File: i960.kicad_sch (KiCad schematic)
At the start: 48 parts

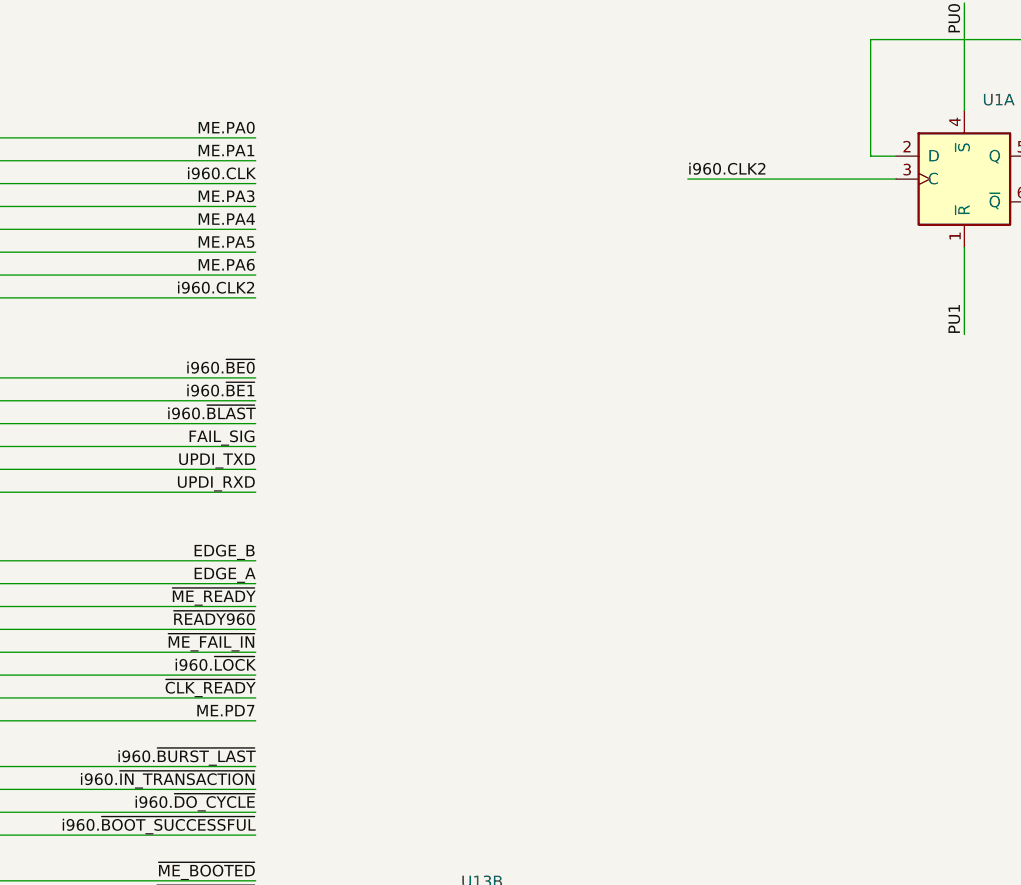
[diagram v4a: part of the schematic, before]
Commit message: Added a new 9 pin breakout header for me pins
PORTA on the ME is now free. CLK is now connected to PD7. That way I can
reuse all of PORTA for whatever I want in the future.
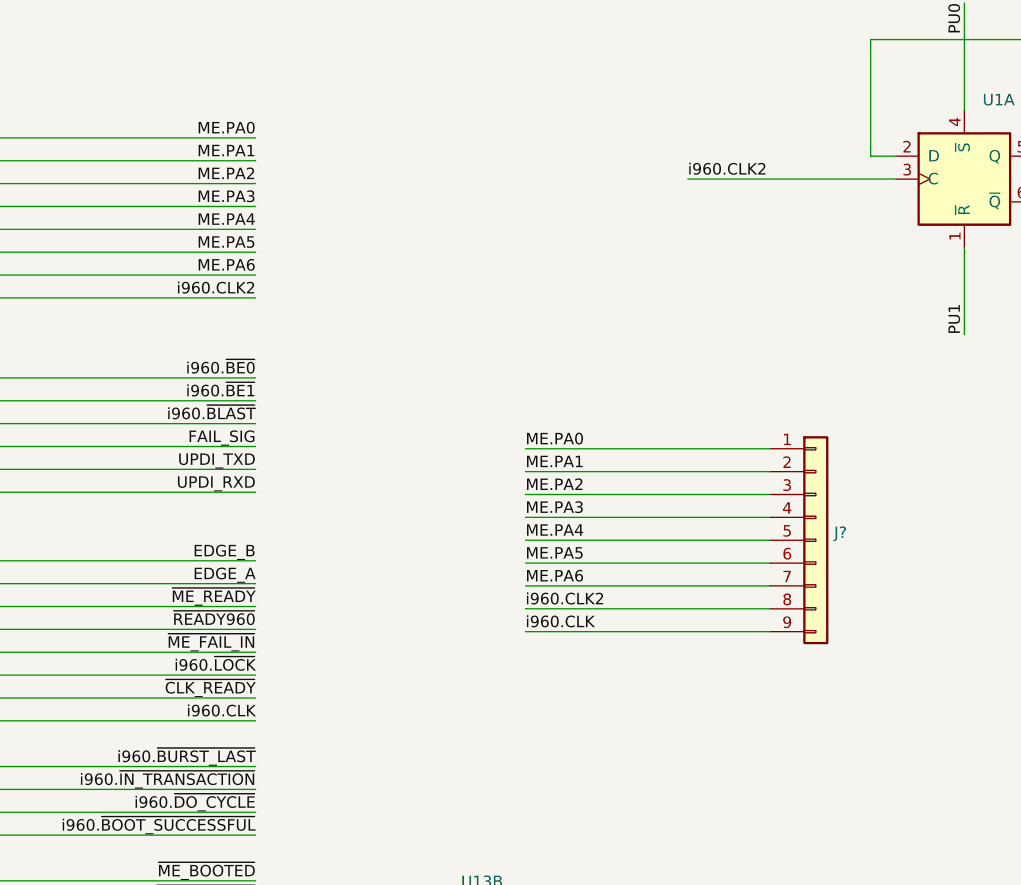
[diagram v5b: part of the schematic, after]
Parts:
- added J?: (no value), symbol Connector_Generic:Conn_01x09
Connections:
- net ME.PD7 is gone; now on net i960.CLK: U16.16 ((AIN7/AREF)PD7)
- net ME.PA0: now also J?.1 (Pin_1)
- net ME.PA1: now also J?.2 (Pin_2)
- net ME.PA3: now also J?.4 (Pin_4)
- net ME.PA4: now also J?.5 (Pin_5)
- net ME.PA5: now also J?.6 (Pin_6)
- net ME.PA6: now also J?.7 (Pin_7)
- net i960.CLK: now also J?.9 (Pin_9); no longer U16.35 ((XCK0/SDA/CCL0-IN2)PA2)
- net i960.CLK2: now also J?.8 (Pin_8)
- new net ME.PA2: J?.3 (Pin_3), U16.35 ((XCK0/SDA/CCL0-IN2)PA2)
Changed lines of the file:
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@@
+    (stroke (width 0) (type default) (color 0 0 0 0))
+  )
+  (wire (pts (xy 172.466 84.582) (xy 199.644 84.582))
     (stroke (width 0) (type default) (color 0 0 0 0))
   )
@@
     (stroke (width 0) (type default) (color 0 0 0 0))
   )
+  (wire (pts (xy 172.466 76.962) (xy 199.644 76.962))
+    (stroke (width 0) (type default) (color 0 0 0 0))
+  )
   (wire (pts (xy 514.604 80.264) (xy 542.29 80.264))
     (stroke (width 0) (type default) (color 0 0 0 0))
@@
     (stroke (width 0) (type default) (color 0 0 0 0))
   )
+  (wire (pts (xy 172.466 89.662) (xy 199.644 89.662))
+    (stroke (width 0) (type default) (color 0 0 0 0))
+  )
   (wire (pts (xy 45.212 135.128) (xy 45.212 118.11))
     (stroke (width 0) (type default) (color 0 0 0 0))
@@
     (stroke (width 0) (type default) (color 0 0 0 0))
   )
+  (wire (pts (xy 172.466 79.502) (xy 199.644 79.502))
+    (stroke (width 0) (type default) (color 0 0 0 0))
+  )
   (wire (pts (xy 210.312 462.788) (xy 210.312 427.736))
     (stroke (width 0) (type default) (color 0 0 0 0))
@@
     (stroke (width 0) (type default) (color 0 0 0 0))
   )
+  (wire (pts (xy 172.466 97.282) (xy 199.644 97.282))
+    (stroke (width 0) (type default) (color 0 0 0 0))
+  )
   (wire (pts (xy 59.69 61.468) (xy 20.066 61.468))
     (stroke (width 0) (type default) (color 0 0 0 0))
@@
     (stroke (width 0) (type default) (color 0 0 0 0))
   )
+  (wire (pts (xy 172.466 82.042) (xy 199.644 82.042))
+    (stroke (width 0) (type default) (color 0 0 0 0))
+  )
   (wire (pts (xy 23.876 364.236) (xy 54.102 364.236))
     (stroke (width 0) (type default) (color 0 0 0 0))
@@
     (stroke (width 0) (type default) (color 0 0 0 0))
   )
+  (wire (pts (xy 172.466 94.742) (xy 199.644 94.742))
+    (stroke (width 0) (type default) (color 0 0 0 0))
+  )
   (wire (pts (xy 467.106 57.404) (xy 502.92 57.404))
     (stroke (width 0) (type default) (color 0 0 0 0))
@@
     (stroke (width 0) (type default) (color 0 0 0 0))
   )
+  (wire (pts (xy 172.466 92.202) (xy 199.644 92.202))
+    (stroke (width 0) (type default) (color 0 0 0 0))
+  )
   (wire (pts (xy 346.71 266.446) (xy 377.698 266.446))
     (stroke (width 0) (type default) (color 0 0 0 0))
@@
   )
   (wire (pts (xy 148.336 25.4) (xy 169.164 25.4))
+    (stroke (width 0) (type default) (color 0 0 0 0))
+  )
+  (wire (pts (xy 172.466 87.122) (xy 199.644 87.122))
     (stroke (width 0) (type default) (color 0 0 0 0))
   )
@@
     (effects (font (size 1.27 1.27)) (justify left bottom))
   )
+  (label "ME.PA4" (at 172.466 87.122 0)
+    (effects (font (size 1.27 1.27)) (justify left bottom))
+  )
   (label "~{RESET_INTERMEDIATE}" (at 142.494 132.588 180)
     (effects (font (size 1.27 1.27)) (justify right bottom))
@@
     (effects (font (size 1.27 1.27)) (justify right bottom))
   )
+  (label "ME.PA0" (at 172.466 76.962 0)
+    (effects (font (size 1.27 1.27)) (justify left bottom))
+  )
   (label "AD1" (at 405.892 44.704 0)
     (effects (font (size 1.27 1.27)) (justify left bottom))
@@
     (effects (font (size 1.27 1.27)) (justify left bottom))
   )
+  (label "ME.PA1" (at 172.466 79.502 0)
+    (effects (font (size 1.27 1.27)) (justify left bottom))
+  )
   (label "i960.D0" (at 489.966 170.942 0)
     (effects (font (size 1.27 1.27)) (justify left bottom))
@@
     (effects (font (size 1.27 1.27)) (justify left bottom))
   )
+  (label "i960.CLK2" (at 172.466 94.742 0)
+    (effects (font (size 1.27 1.27)) (justify left bottom))
+  )
   (label "PU3" (at 294.386 119.634 90)
     (effects (font (size 1.27 1.27)) (justify left bottom))
@@
     (effects (font (size 1.27 1.27)) (justify right bottom))
   )
+  (label "ME.PA2" (at 142.494 47.498 180)
+    (effects (font (size 1.27 1.27)) (justify right bottom))
+  )
   (label "PU0" (at 221.234 27.432 270)
     (effects (font (size 1.27 1.27)) (justify right bottom))
@@
     (effects (font (size 1.27 1.27)) (justify right bottom))
   )
+  (label "ME.PA5" (at 172.466 89.662 0)
+    (effects (font (size 1.27 1.27)) (justify left bottom))
+  )
   (label "AD6" (at 405.892 57.404 0)
     (effects (font (size 1.27 1.27)) (justify left bottom))
@@
     (effects (font (size 1.27 1.27)) (justify left bottom))
   )
-  (label "i960.CLK" (at 142.494 47.498 180)
+  (label "i960.CLK" (at 142.494 107.188 180)
     (effects (font (size 1.27 1.27)) (justify right bottom))
   )
@@
     (effects (font (size 1.27 1.27)) (justify right bottom))
   )
+  (label "ME.PA3" (at 172.466 84.582 0)
+    (effects (font (size 1.27 1.27)) (justify left bottom))
+  )
   (label "i960.A21" (at 515.874 72.644 0)
     (effects (font (size 1.27 1.27)) (justify left bottom))
@@
     (effects (font (size 1.27 1.27)) (justify right bottom))
   )
+  (label "ME.PA2" (at 172.466 82.042 0)
+    (effects (font (size 1.27 1.27)) (justify left bottom))
+  )
   (label "i960.CLK2" (at 514.604 28.448 0)
     (effects (font (size 1.27 1.27)) (justify left bottom))
@@
     (effects (font (size 1.27 1.27)) (justify left bottom))
   )
-  (label "ME.PD7" (at 142.494 107.188 180)
-    (effects (font (size 1.27 1.27)) (justify right bottom))
-  )
   (label "AD13" (at 380.492 186.436 0)
     (effects (font (size 1.27 1.27)) (justify left bottom))
@@
     (effects (font (size 1.27 1.27)) (justify right bottom))
   )
+  (label "i960.CLK" (at 172.466 97.282 0)
+    (effects (font (size 1.27 1.27)) (justify left bottom))
+  )
   (label "i960.~{AS}" (at 570.738 173.482 180)
     (effects (font (size 1.27 1.27)) (justify right bottom))
@@
   )
   (label "i960.~{INT0}" (at 450.342 393.954 0)
+    (effects (font (size 1.27 1.27)) (justify left bottom))
+  )
+  (label "ME.PA6" (at 172.466 92.202 0)
     (effects (font (size 1.27 1.27)) (justify left bottom))
   )
@@
     (pin "1")
   )
+  (symbol (lib_id "Connector_Generic:Conn_01x09") (at 204.724 87.122 0) (unit 1)
+    (in_bom yes) (on_board yes) (fields_autoplaced)
+    (property "Reference" "J?" (id 0) (at 206.756 86.2873 0)
+      (effects (font (size 1.27 1.27)) (justify left))
+    )
+    (property "Value" "" (id 1) (at 206.756 88.8242 0)
+      (effects (font (size 1.27 1.27)) (justify left))
+    )
+    (property "Footprint" "" (id 2) (at 204.724 87.122 0)
+      (effects (font (size 1.27 1.27)) hide)
+    )
+    (property "Datasheet" "~" (id 3) (at 204.724 87.122 0)
+      (effects (font (size 1.27 1.27)) hide)
+    )
+    (pin "1")
+    (pin "2")
+    (pin "3")
+    (pin "4")
+    (pin "5")
+    (pin "6")
+    (pin "7")
+    (pin "8")
+    (pin "9")
+  )
   (symbol (lib_id "power:GND") (at 260.096 182.118 0) (unit 1)
